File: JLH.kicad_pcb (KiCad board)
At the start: 2 copper layers, 170 x 202 mm, 41 parts, among them J1 Вход, J2 Выход, J3 B2P-VH, Q1 КТ361Г, Q2 КТ801А, Q3 2Т803А, Q4 2Т803А, Q5 КТ361Г, Q6 КТ801А, Q7 2Т803А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

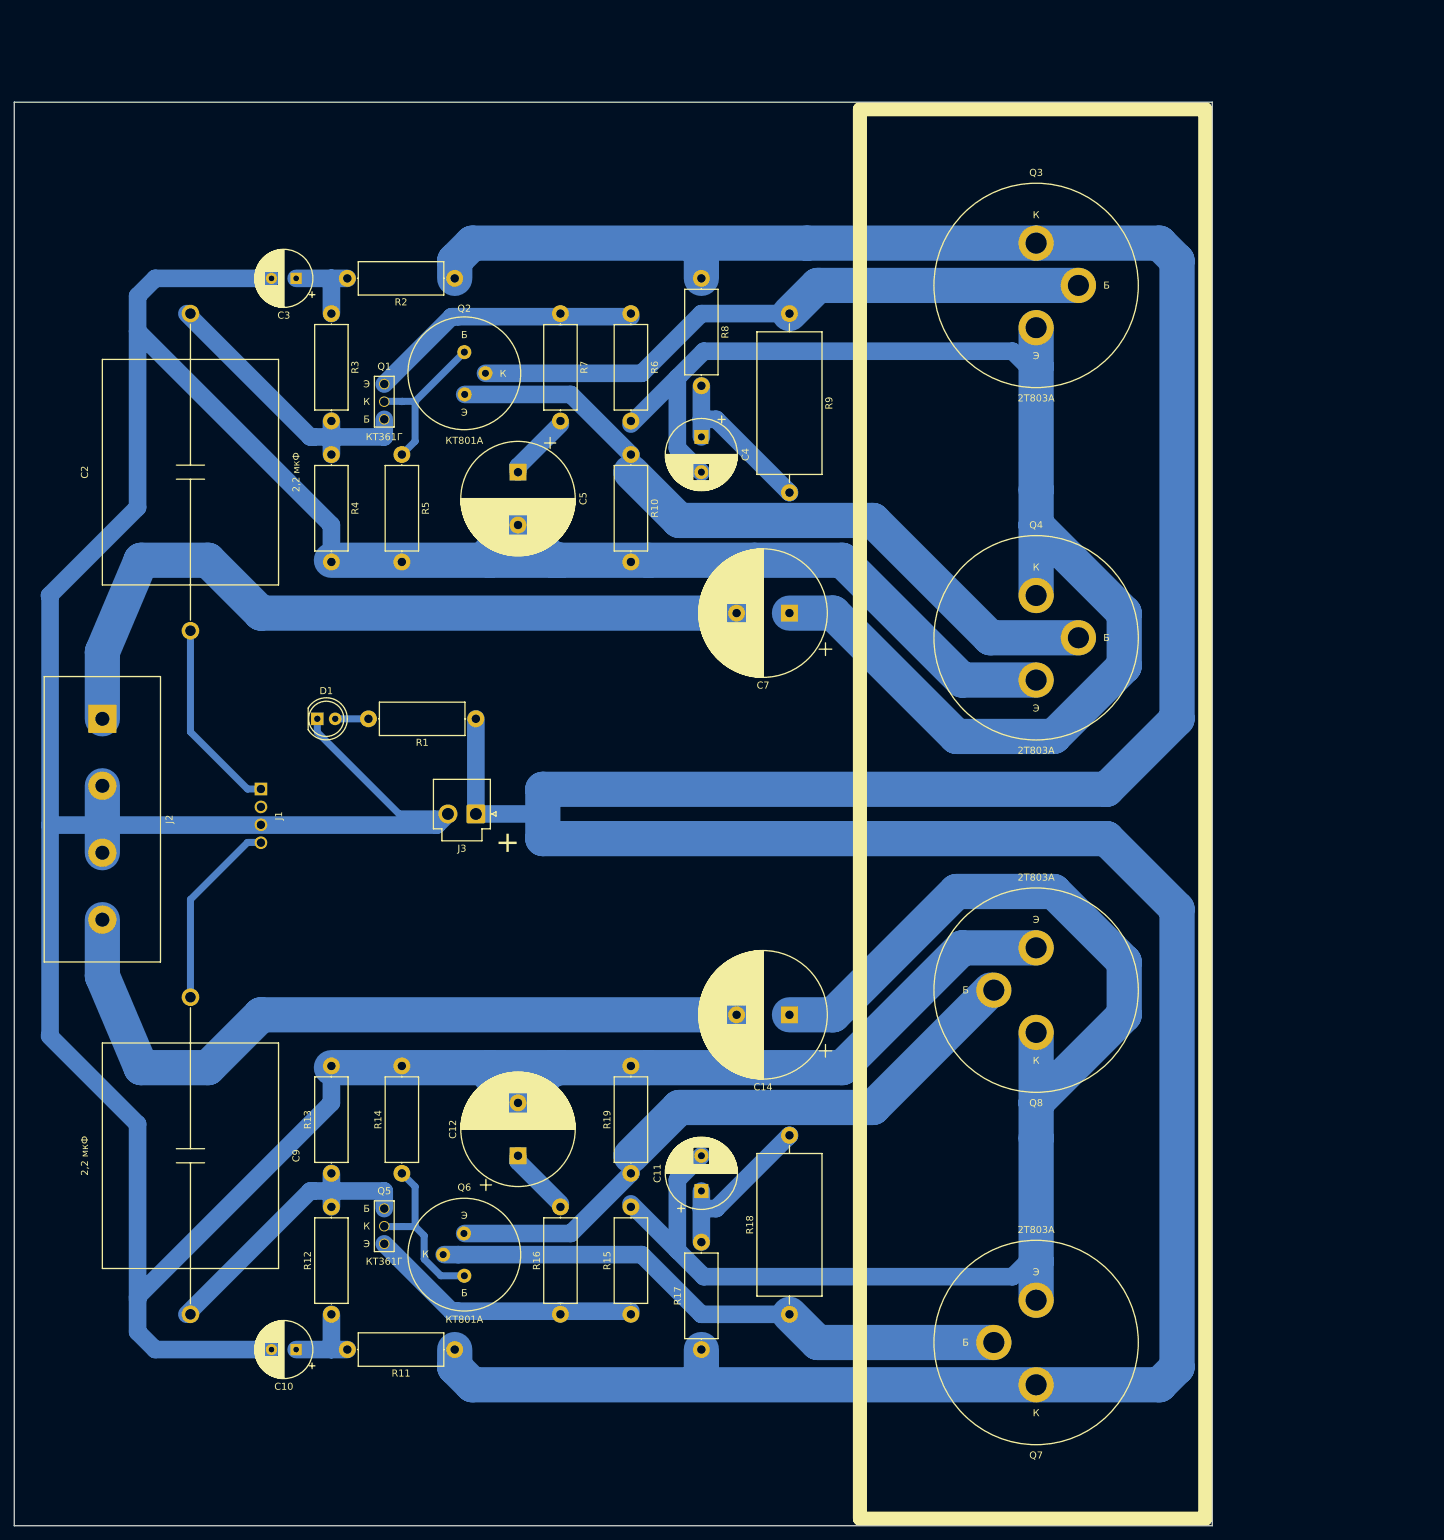
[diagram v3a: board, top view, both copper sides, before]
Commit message: Added filled zones
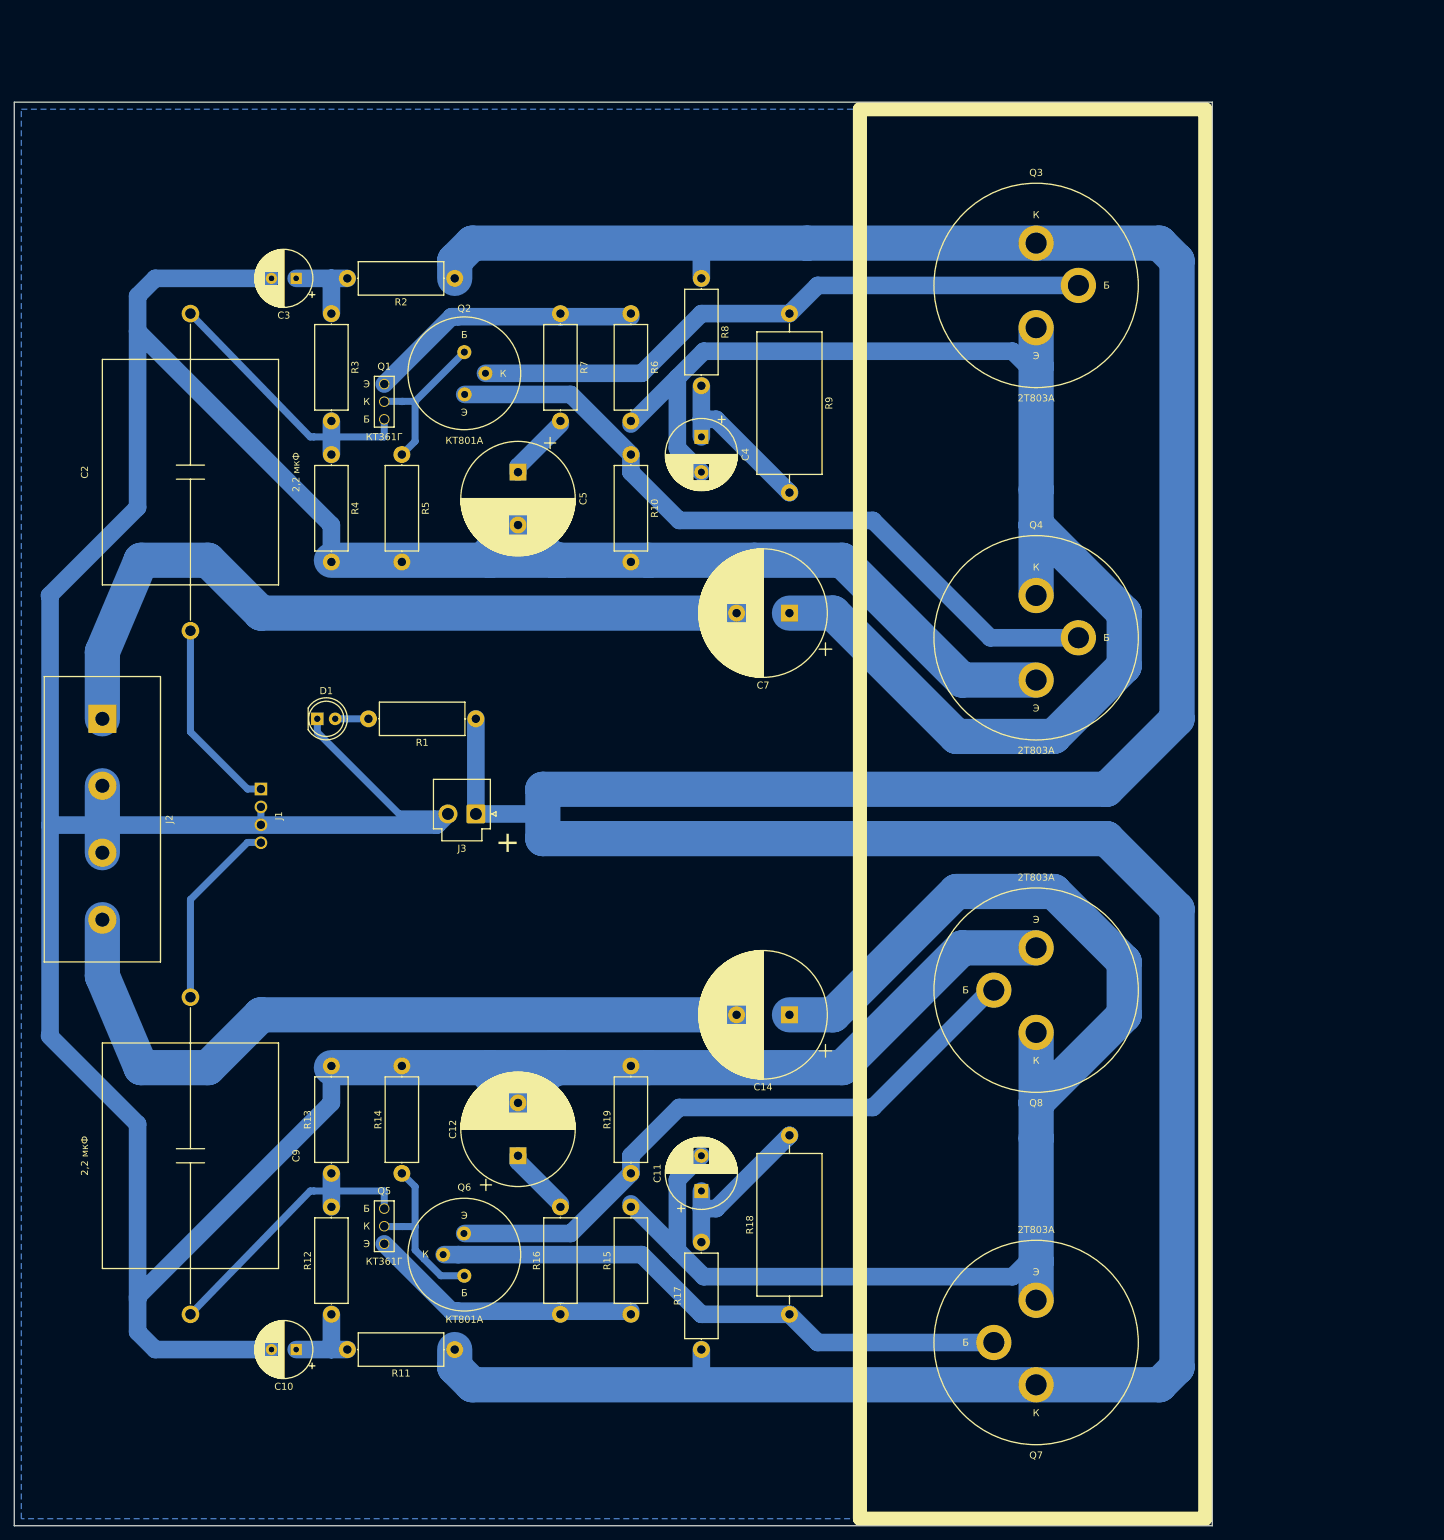
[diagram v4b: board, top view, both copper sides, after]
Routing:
- net GND: track 621.1 -> 623.6 mm
- added copper zone on B.Cu, net GND

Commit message: Added mounting holes
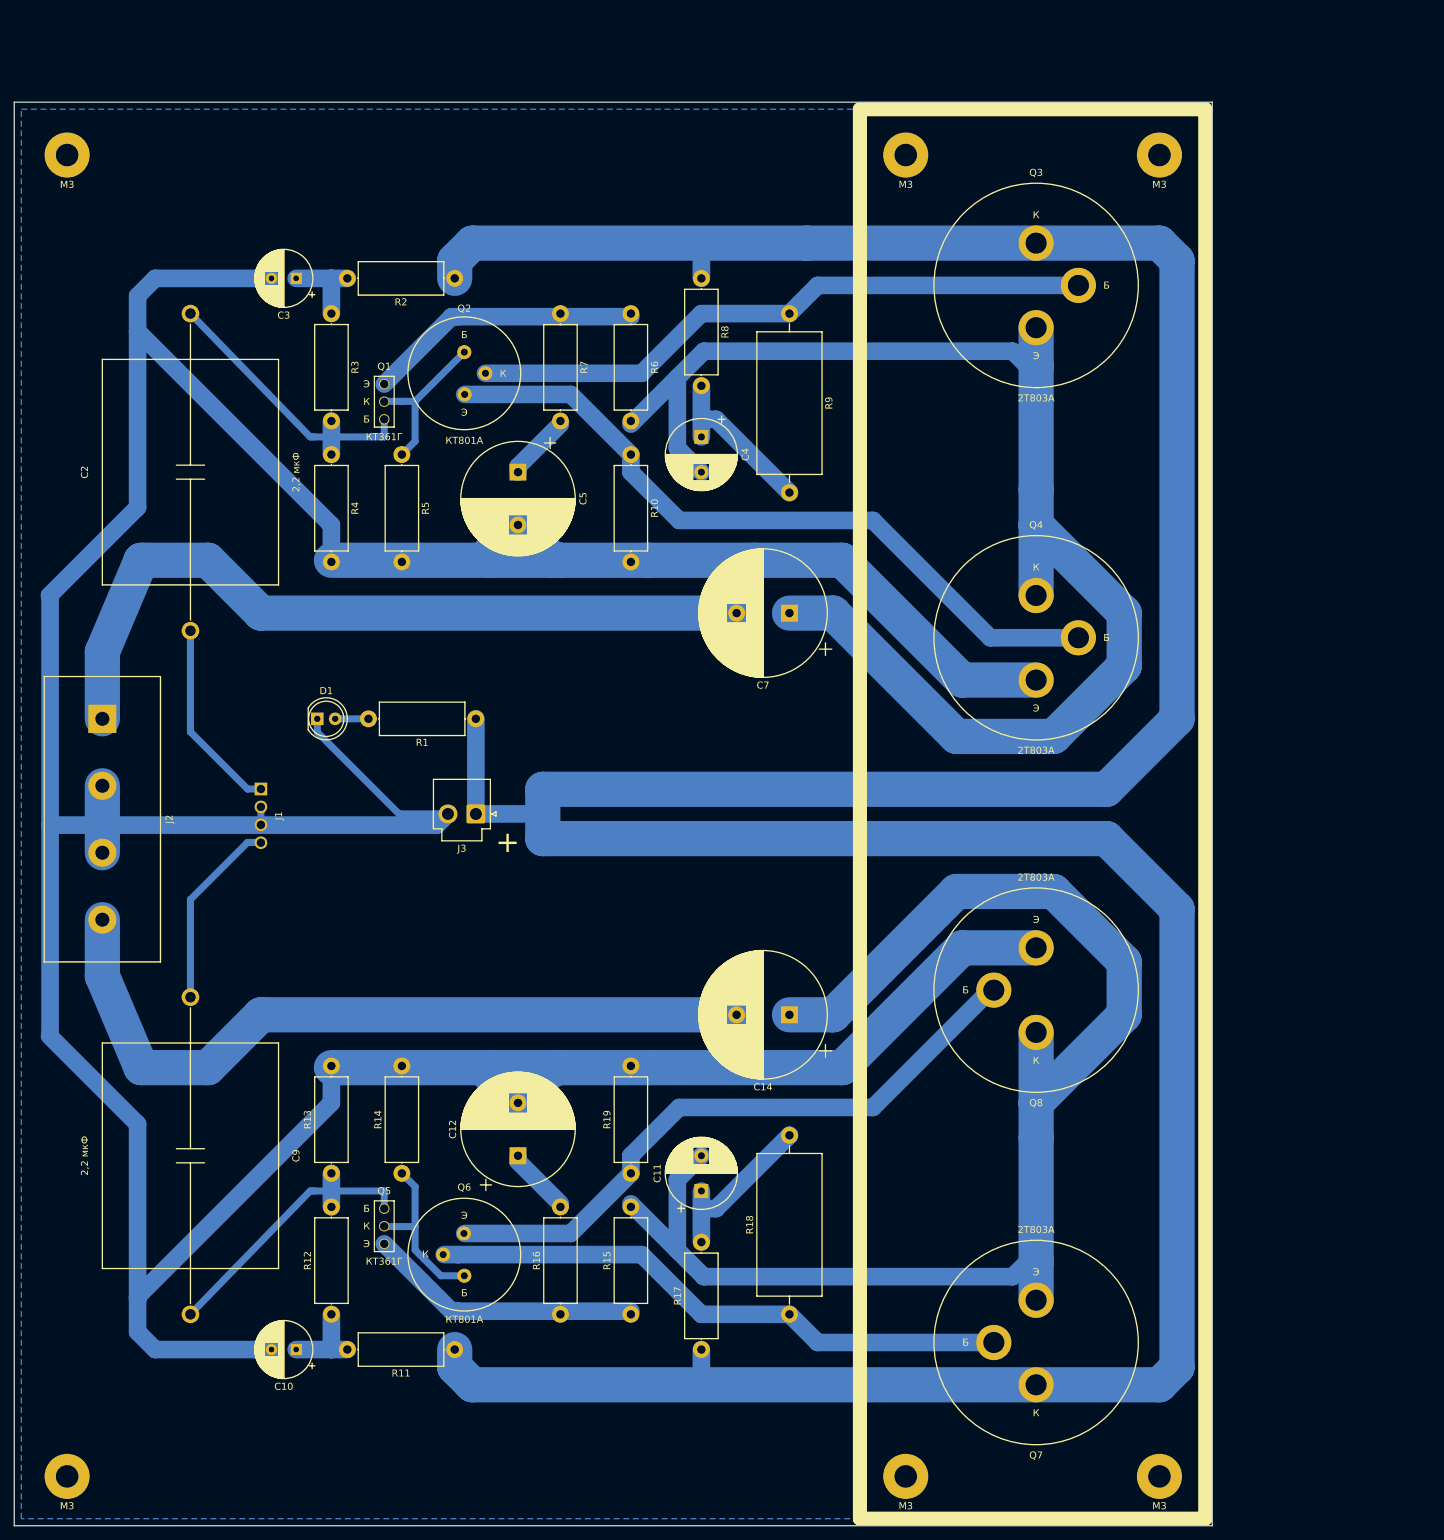
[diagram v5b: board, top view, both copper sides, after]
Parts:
- added H1: M3, MountingHole:MountingHole_3.2mm_M3_Pad, F.Cu at (27.5, 32.5)
- added H2: M3, MountingHole:MountingHole_3.2mm_M3_Pad, F.Cu at (27.5, 220.0)
- added H3: M3, MountingHole:MountingHole_3.2mm_M3_Pad, F.Cu at (146.5, 32.5)
- added H4: M3, MountingHole:MountingHole_3.2mm_M3_Pad, F.Cu at (146.5, 220.0)
- added H5: M3, MountingHole:MountingHole_3.2mm_M3_Pad, F.Cu at (182.5, 32.5)
- added H6: M3, MountingHole:MountingHole_3.2mm_M3_Pad, F.Cu at (182.5, 220.0)
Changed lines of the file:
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@@
   (general
     (thickness 1.6)
-    (drawings 17)
+    (drawings 16)
     (tracks 202)
     (zones 0)
-    (modules 41)
+    (modules 47)
     (nets 26)
   )
@@
     )
   )
+  (module MountingHole:MountingHole_3.2mm_M3_Pad (layer F.Cu)
+    (at 27.5 32.5)
+    (descr "Mounting Hole 3.2mm, M3")
+    (tags "mounting hole 3.2mm m3")
+    (attr virtual)
+    (fp_text reference H1 (at 0 -4.2) (layer F.SilkS) hide
+      (effects (font (size 1 1) (thickness 0.15)))
+    )
+    (fp_text value M3 (at 0 4.2) (layer F.SilkS)
+      (effects (font (size 1 1) (thickness 0.15)))
+    )
+    (fp_text user %R (at 0.3 0) (layer F.Fab)
+      (effects (font (size 1 1) (thickness 0.15)))
+    )
+    (fp_circle (center 0 0) (end 3.2 0) (layer Cmts.User) (width 0.15))
+    (fp_circle (center 0 0) (end 3.45 0) (layer F.CrtYd) (width 0.05))
+    (pad 1 thru_hole circle (at 0 0) (size 6.4 6.4) (drill 3.2) (layers *.Cu *.Mask))
+  )
+  (module MountingHole:MountingHole_3.2mm_M3_Pad (layer F.Cu)
+    (at 27.5 220)
+    (descr "Mounting Hole 3.2mm, M3")
+    (tags "mounting hole 3.2mm m3")
+    (attr virtual)
+    (fp_text reference H2 (at 0 -4.2) (layer F.SilkS) hide
+      (effects (font (size 1 1) (thickness 0.15)))
+    )
+    (fp_text value M3 (at 0 4.2) (layer F.SilkS)
+      (effects (font (size 1 1) (thickness 0.15)))
+    )
+    (fp_text user %R (at 0.3 0) (layer F.Fab)
+      (effects (font (size 1 1) (thickness 0.15)))
+    )
+    (fp_circle (center 0 0) (end 3.2 0) (layer Cmts.User) (width 0.15))
+    (fp_circle (center 0 0) (end 3.45 0) (layer F.CrtYd) (width 0.05))
+    (pad 1 thru_hole circle (at 0 0) (size 6.4 6.4) (drill 3.2) (layers *.Cu *.Mask))
+  )
+  (module MountingHole:MountingHole_3.2mm_M3_Pad (layer F.Cu)
+    (at 146.5 32.5)
+    (descr "Mounting Hole 3.2mm, M3")
+    (tags "mounting hole 3.2mm m3")
+    (attr virtual)
+    (fp_text reference H3 (at 0 -4.2) (layer F.SilkS) hide
+      (effects (font (size 1 1) (thickness 0.15)))
+    )
+    (fp_text value M3 (at 0 4.2) (layer F.SilkS)
+      (effects (font (size 1 1) (thickness 0.15)))
+    )
+    (fp_text user %R (at 0.3 0) (layer F.Fab)
+      (effects (font (size 1 1) (thickness 0.15)))
+    )
+    (fp_circle (center 0 0) (end 3.2 0) (layer Cmts.User) (width 0.15))
+    (fp_circle (center 0 0) (end 3.45 0) (layer F.CrtYd) (width 0.05))
+    (pad 1 thru_hole circle (at 0 0) (size 6.4 6.4) (drill 3.2) (layers *.Cu *.Mask))
+  )
+  (module MountingHole:MountingHole_3.2mm_M3_Pad (layer F.Cu)
+    (at 146.5 220)
+    (descr "Mounting Hole 3.2mm, M3")
+    (tags "mounting hole 3.2mm m3")
+    (attr virtual)
+    (fp_text reference H4 (at 0 -4.2) (layer F.SilkS) hide
+      (effects (font (size 1 1) (thickness 0.15)))
+    )
+    (fp_text value M3 (at 0 4.2) (layer F.SilkS)
+      (effects (font (size 1 1) (thickness 0.15)))
+    )
+    (fp_text user %R (at 0.3 0) (layer F.Fab)
+      (effects (font (size 1 1) (thickness 0.15)))
+    )
+    (fp_circle (center 0 0) (end 3.2 0) (layer Cmts.User) (width 0.15))
+    (fp_circle (center 0 0) (end 3.45 0) (layer F.CrtYd) (width 0.05))
+    (pad 1 thru_hole circle (at 0 0) (size 6.4 6.4) (drill 3.2) (layers *.Cu *.Mask))
+  )
+  (module MountingHole:MountingHole_3.2mm_M3_Pad (layer F.Cu)
+    (at 182.5 32.5)
+    (descr "Mounting Hole 3.2mm, M3")
+    (tags "mounting hole 3.2mm m3")
+    (attr virtual)
+    (fp_text reference H5 (at 0 -4.2) (layer F.SilkS) hide
+      (effects (font (size 1 1) (thickness 0.15)))
+    )
+    (fp_text value M3 (at 0 4.2) (layer F.SilkS)
+      (effects (font (size 1 1) (thickness 0.15)))
+    )
+    (fp_circle (center 0 0) (end 3.45 0) (layer F.CrtYd) (width 0.05))
+    (fp_circle (center 0 0) (end 3.2 0) (layer Cmts.User) (width 0.15))
+    (fp_text user %R (at 0.3 0) (layer F.Fab)
+      (effects (font (size 1 1) (thickness 0.15)))
+    )
+    (pad 1 thru_hole circle (at 0 0) (size 6.4 6.4) (drill 3.2) (layers *.Cu *.Mask))
+  )
+  (module MountingHole:MountingHole_3.2mm_M3_Pad (layer F.Cu)
+    (at 182.5 220)
+    (descr "Mounting Hole 3.2mm, M3")
+    (tags "mounting hole 3.2mm m3")
+    (attr virtual)
+    (fp_text reference H6 (at 0 -4.2) (layer F.SilkS) hide
+      (effects (font (size 1 1) (thickness 0.15)))
+    )
+    (fp_text value M3 (at 0 4.2) (layer F.SilkS)
+      (effects (font (size 1 1) (thickness 0.15)))
+    )
+    (fp_circle (center 0 0) (end 3.45 0) (layer F.CrtYd) (width 0.05))
+    (fp_circle (center 0 0) (end 3.2 0) (layer Cmts.User) (width 0.15))
+    (fp_text user %R (at 0.3 0) (layer F.Fab)
+      (effects (font (size 1 1) (thickness 0.15)))
+    )
+    (pad 1 thru_hole circle (at 0 0) (size 6.4 6.4) (drill 3.2) (layers *.Cu *.Mask))
+  )
   (gr_line (start 20 227) (end 20 25) (layer Edge.Cuts) (width 0.05))
   (gr_line (start 190 227) (end 20 227) (layer Edge.Cuts) (width 0.05))
@@
     (arrow2b (pts (xy 165 32.5) (xy 166.126504 31.913579)))
   )
-  (dimension 25 (width 0.15) (layer Eco2.User)
-    (gr_text "25.000 mm" (at 152.5 31.2) (layer Eco2.User)
-      (effects (font (size 1 1) (thickness 0.15)))
-    )
-    (feature1 (pts (xy 140 45) (xy 140 31.913579)))
-    (feature2 (pts (xy 165 45) (xy 165 31.913579)))
-    (crossbar (pts (xy 165 32.5) (xy 140 32.5)))
-    (arrow1a (pts (xy 140 32.5) (xy 141.126504 31.913579)))
-    (arrow1b (pts (xy 140 32.5) (xy 141.126504 33.086421)))
-    (arrow2a (pts (xy 165 32.5) (xy 163.873496 31.913579)))
-    (arrow2b (pts (xy 165 32.5) (xy 163.873496 33.086421)))
-  )
   (dimension 50 (width 0.15) (layer Eco2.User)
     (gr_text "50.000 mm" (at 165 28.8) (layer Eco2.User)
@@
   (segment (start 32.5 131.5) (end 32.5 127.5) (width 5) (layer B.Cu) (net 4) (status 10))
   (segment (start 32.5 122) (end 32.5 127.5) (width 5) (layer B.Cu) (net 4) (status 10))
-  (segment (start 55 125) (end 55 127.54) (width 1) (layer B.Cu) (net 4))
+  (segment (start 55 125) (end 55 127.54) (width 1) (layer B.Cu) (net 4) (status 30))
   (segment (start 129.8 80.2) (end 130 80.4) (width 2.5) (layer B.Cu) (net 5) (status 30))
   (segment (start 119.6 70) (end 130 80.4) (width 2.5) (layer B.Cu) (net 5) (status 20))
